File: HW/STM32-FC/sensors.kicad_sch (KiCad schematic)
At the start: 18 parts, among them J5 JST ZH 1.5mm 2P, U6 BMI323, U7 ICM-42688-P, U8 LIS2MDLTR, U9 LPS22HH

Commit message: 2025.02.06 PCB routing done v2
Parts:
- C21, C23, C28, C29: LCSC C1525 -> C1581
- C22: LCSC C1525 -> C26409
- C24: LCSC C1525 -> C1531
- C26: LCSC (none) -> C29823
- C27: LCSC C1525 -> C40894
- C30: LCSC C1525 -> C1770
- J5: LCSC (none) -> C265329
- R16: LCSC (none) -> C25531
- R17: LCSC (none) -> C25539
- R18: LCSC (none) -> C11702
- U6: LCSC (none) -> C5368700
- U7: LCSC (none) -> C1850418
- U8: LCSC (none) -> C919695
- U9: LCSC (none) -> C2827824
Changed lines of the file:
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@@
 			)
 		)
-		(property "LCSC" "C1525"
+		(property "LCSC" "C1531"
 			(at 102.87 40.6462 0)
 			(effects
@@
 			)
 		)
+		(property "LCSC" "C265329"
+			(at 219.71 68.58 0)
+			(effects
+				(font
+					(size 1.27 1.27)
+				)
+				(hide yes)
+			)
+		)
 		(pin "1"
 		)
@@
 			)
 		)
-		(property "LCSC" "C1525"
+		(property "LCSC" "C1581"
 			(at 49.53 128.2762 0)
 			(effects
@@
 			)
 		)
+		(property "LCSC" "C25539"
+			(at 236.22 34.29 0)
+			(effects
+				(font
+					(size 1.27 1.27)
+				)
+				(hide yes)
+			)
+		)
 		(pin "1"
 		)
@@
 			)
 		)
-		(property "LCSC" "C1525"
+		(property "LCSC" "C1770"
 			(at 182.88 68.5862 0)
 			(effects
@@
 			)
 		)
-		(property "LCSC" "C1525"
+		(property "LCSC" "C26409"
 			(at 92.71 40.6462 0)
 			(effects
@@
 			)
 		)
-		(property "LCSC" "C1525"
+		(property "LCSC" "C1581"
 			(at 93.98 137.1538 0)
 			(effects
@@
 			)
 		)
+		(property "LCSC" "C29823"
+			(at 147.32 125.73 0)
+			(effects
+				(font
+					(size 1.27 1.27)
+				)
+				(hide yes)
+			)
+		)
 		(pin "2"
 		)
@@
 			)
 		)
+		(property "LCSC" "C1850418"
+			(at 64.77 50.8 0)
+			(effects
+				(font
+					(size 1.27 1.27)
+				)
+				(hide yes)
+			)
+		)
 		(pin "7"
 		)
@@
 			)
 		)
-		(property "LCSC" "C1525"
+		(property "LCSC" "C1581"
 			(at 181.61 33.0262 0)
 			(effects
@@
 			)
 		)
+		(property "LCSC" "C919695"
+			(at 157.48 64.77 0)
+			(effects
+				(font
+					(size 1.27 1.27)
+				)
+				(hide yes)
+			)
+		)
 		(pin "1"
 		)
@@
 			)
 		)
+		(property "LCSC" "C25531"
+			(at 189.23 121.92 0)
+			(effects
+				(font
+					(size 1.27 1.27)
+				)
+				(hide yes)
+			)
+		)
 		(pin "1"
 		)
@@
 			)
 		)
+		(property "LCSC" "C2827824"
+			(at 161.29 127 0)
+			(effects
+				(font
+					(size 1.27 1.27)
+				)
+				(hide yes)
+			)
+		)
 		(pin "7"
 		)
@@
 			)
 		)
-		(property "LCSC" "C1525"
+		(property "LCSC" "C40894"
 			(at 158.75 33.0262 0)
 			(effects
@@
 			)
 		)
+		(property "LCSC" "C5368700"
+			(at 53.34 115.57 0)
+			(effects
+				(font
+					(size 1.27 1.27)
+				)
+				(hide yes)
+			)
+		)
 		(pin "13"
 		)
@@
 			)
 		)
-		(property "LCSC" "C1525"
+		(property "LCSC" "C1581"
 			(at 170.18 33.0262 0)
 			(effects
@@
 			(at 236.22 44.45 0)
 			(effects
+				(font
+					(size 1.27 1.27)
+				)
+				(hide yes)
+			)
+		)
+		(property "LCSC" "C11702"
+			(at 236.22 44.45 0)
+			(effects

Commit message: 2025.02.06 PCB routing done v3
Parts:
- C25: LCSC C1525 -> C1524
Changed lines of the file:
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@@
 			)
 		)
+		(property "JLC" ""
+			(at 100.33 41.91 0)
+			(effects
+				(font
+					(size 1.27 1.27)
+				)
+				(hide yes)
+			)
+		)
 		(pin "1"
 		)
@@
 			)
 		)
+		(property "JLC" ""
+			(at 219.71 68.58 0)
+			(effects
+				(font
+					(size 1.27 1.27)
+				)
+				(hide yes)
+			)
+		)
 		(pin "1"
 		)
@@
 			)
 		)
+		(property "JLC" ""
+			(at 46.99 129.54 0)
+			(effects
+				(font
+					(size 1.27 1.27)
+				)
+				(hide yes)
+			)
+		)
 		(pin "1"
 		)
@@
 			)
 		)
+		(property "JLC" ""
+			(at 236.22 34.29 0)
+			(effects
+				(font
+					(size 1.27 1.27)
+				)
+				(hide yes)
+			)
+		)
 		(pin "1"
 		)
@@
 			)
 		)
-		(property "LCSC" "C1525"
+		(property "LCSC" "C1524"
 			(at 113.03 40.6462 0)
 			(effects
@@
 			)
 		)
+		(property "JLC" ""
+			(at 110.49 41.91 0)
+			(effects
+				(font
+					(size 1.27 1.27)
+				)
+				(hide yes)
+			)
+		)
 		(pin "1"
 		)
@@
 			)
 		)
+		(property "JLC" ""
+			(at 180.34 69.85 0)
+			(effects
+				(font
+					(size 1.27 1.27)
+				)
+				(hide yes)
+			)
+		)
 		(pin "1"
 		)
@@
 			)
 		)
+		(property "JLC" ""
+			(at 90.17 41.91 0)
+			(effects
+				(font
+					(size 1.27 1.27)
+				)
+				(hide yes)
+			)
+		)
 		(pin "1"
 		)
@@
 			)
 		)
+		(property "JLC" ""
+			(at 96.52 135.89 0)
+			(effects
+				(font
+					(size 1.27 1.27)
+				)
+				(hide yes)
+			)
+		)
 		(pin "1"
 		)
@@
 			)
 		)
+		(property "JLC" ""
+			(at 147.32 125.73 0)
+			(effects
+				(font
+					(size 1.27 1.27)
+				)
+				(hide yes)
+			)
+		)
 		(pin "2"
 		)
@@
 			)
 		)
+		(property "JLC" ""
+			(at 64.77 50.8 0)
+			(effects
+				(font
+					(size 1.27 1.27)
+				)
+				(hide yes)
+			)
+		)
 		(pin "7"
 		)
@@
 			)
 		)
+		(property "JLC" ""
+			(at 179.07 34.29 0)
+			(effects
+				(font
+					(size 1.27 1.27)
+				)
+				(hide yes)
+			)
+		)
 		(pin "1"
 		)
@@
 			)
 		)
+		(property "JLC" ""
+			(at 157.48 64.77 0)
+			(effects
+				(font
+					(size 1.27 1.27)
+				)
+				(hide yes)
+			)
+		)
 		(pin "1"
 		)
@@
 			)
 		)
+		(property "JLC" ""
+			(at 189.23 121.92 0)
+			(effects
+				(font
+					(size 1.27 1.27)
+				)
+				(hide yes)
+			)
+		)
 		(pin "1"
 		)
@@
 			)
 		)
+		(property "JLC" ""
+			(at 161.29 127 0)
+			(effects
+				(font
+					(size 1.27 1.27)
+				)
+				(hide yes)
+			)
+		)
 		(pin "7"
 		)
@@
 			)
 		)
+		(property "JLC" ""
+			(at 156.21 34.29 0)
+			(effects
+				(font
+					(size 1.27 1.27)
+				)
+				(hide yes)
+			)
+		)
 		(pin "1"
 		)
@@
 			)
 		)
+		(property "JLC" ""
+			(at 53.34 115.57 0)
+			(effects
+				(font
+					(size 1.27 1.27)
+				)
+				(hide yes)
+			)
+		)
 		(pin "13"
 		)
@@
 			)
 		)
+		(property "JLC" ""
+			(at 167.64 34.29 0)
+			(effects
+				(font
+					(size 1.27 1.27)
+				)
+				(hide yes)
+			)
+		)
 		(pin "1"
 		)
@@
 			(at 236.22 44.45 0)
 			(effects
+				(font
+					(size 1.27 1.27)
+				)
+				(hide yes)
+			)
+		)
+		(property "JLC" ""
+			(at 236.22 44.45 0)
+			(effects

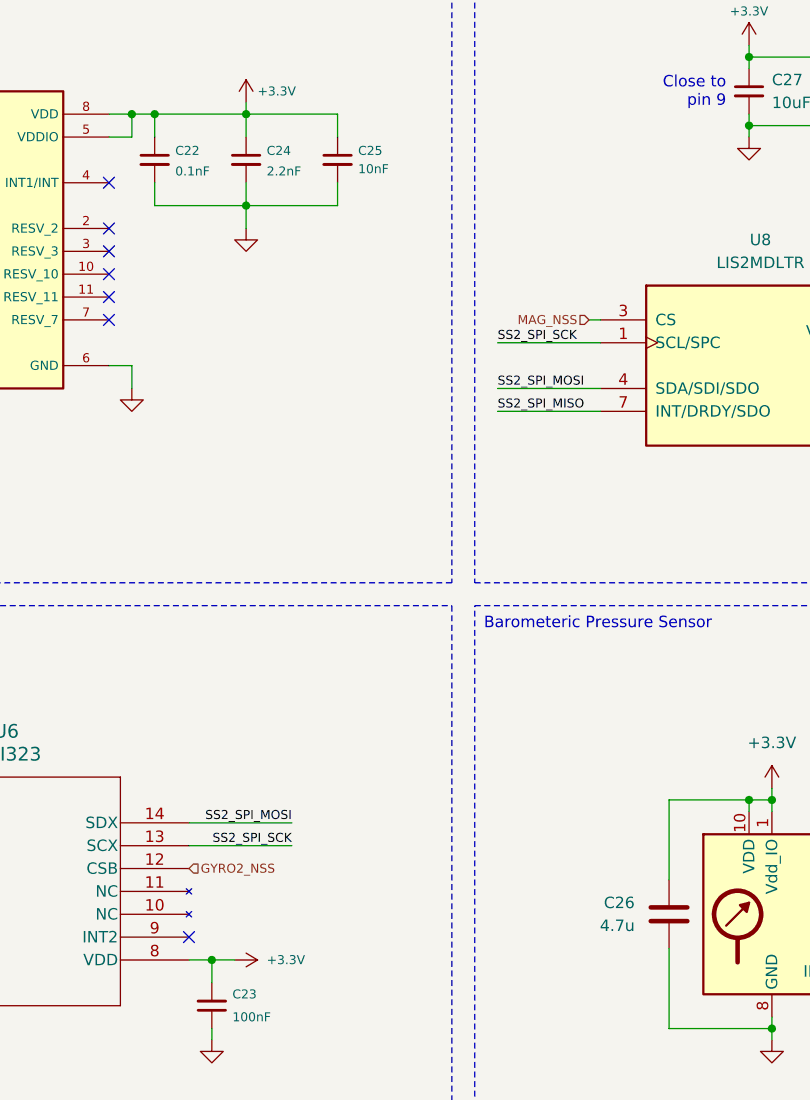
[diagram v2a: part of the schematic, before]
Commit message: 2025.02.07 USB C Conn change v1
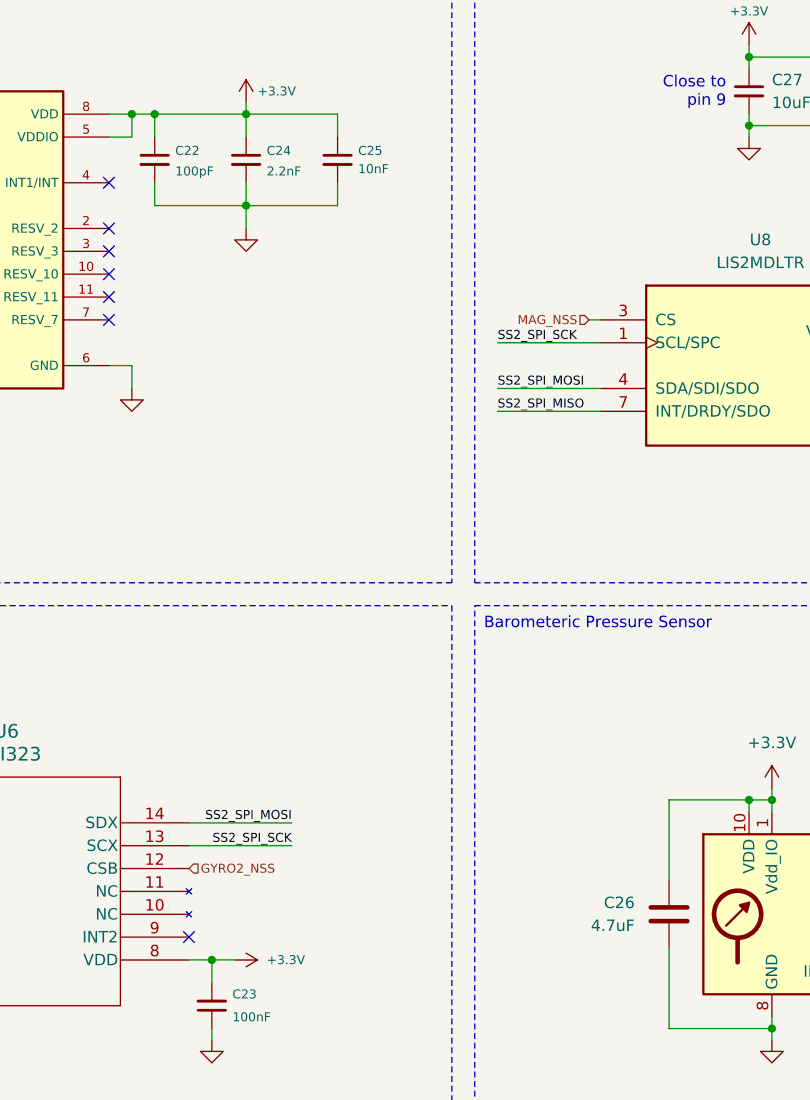
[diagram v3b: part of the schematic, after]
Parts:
- C21, C23, C28, C29: LCSC C1581 -> C1525
- C22: value 0.1nF -> 100pF; LCSC C26409 -> C152819
- C24: LCSC C1531 -> C84703
- C25: LCSC C1524 -> C15195
- C26: value 4.7u -> 4.7uF; LCSC C29823 -> C368809
- C27: LCSC C40894 -> C77000
- C30: LCSC C1770 -> C16651
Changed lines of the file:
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@@
 			)
 		)
-		(property "LCSC" "C1531"
+		(property "LCSC" "C84703"
 			(at 102.87 40.6462 0)
 			(effects
@@
 			)
 		)
-		(property "LCSC" "C1581"
+		(property "LCSC" "C1525"
 			(at 49.53 128.2762 0)
 			(effects
@@
 			)
 		)
-		(property "LCSC" "C1524"
+		(property "LCSC" "C15195"
 			(at 113.03 40.6462 0)
 			(effects
@@
 			)
 		)
-		(property "LCSC" "C1770"
+		(property "LCSC" "C16651"
 			(at 182.88 68.5862 0)
 			(effects
@@
 			)
 		)
-		(property "Value" "0.1nF"
+		(property "Value" "100pF"
 			(at 92.456 43.18 0)
 			(effects
@@
 			)
 		)
-		(property "LCSC" "C26409"
+		(property "LCSC" "C152819"
 			(at 92.71 40.6462 0)
 			(effects
@@
 			)
 		)
-		(property "LCSC" "C1581"
+		(property "LCSC" "C1525"
 			(at 93.98 137.1538 0)
 			(effects
@@
 			)
 		)
-		(property "Value" "4.7u"
+		(property "Value" "4.7uF"
 			(at 143.51 127 0)
 			(effects
@@
 			)
 		)
-		(property "LCSC" "C29823"
+		(property "LCSC" "C368809"
 			(at 147.32 125.73 0)
 			(effects
@@
 			)
 		)
-		(property "LCSC" "C1581"
+		(property "LCSC" "C1525"
 			(at 181.61 33.0262 0)
 			(effects
@@
 			)
 		)
-		(property "LCSC" "C40894"
+		(property "LCSC" "C77000"
 			(at 158.75 33.0262 0)
 			(effects
@@
 			)
 		)
-		(property "LCSC" "C1581"
+		(property "LCSC" "C1525"
 			(at 170.18 33.0262 0)
 			(effects

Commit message: 2025.02.11 PCB DONE! MEMO UPDATING
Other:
- note added: "JST ZH 1.5mm 2P V_BATT : PC0 : ADC123_IN10"
- note added: "SPI1_SCK : PA5 SPI1_MISO : PA6 SPI1_MOSI : PA7 BARO_NSS : PE6 BARO_INT : PE7"
- note added: "SPI1_SCK : PA5 SPI1_MISO : PA6 SPI1_MOSI : PA7 GYRO1_NSS : PE5"
- note added: "SPI3_SCK : PB3 SPI3_MISO : PB4 SPI3_MOSI : PB5 GYRO2_NSS : PE3"
- note added: "SPI3_SCK : PB3 SPI3_MISO : PB4 SPI3_MOSI : PB5 MAG_NSS : PE4"
- note removed: "JST ZH 1.5mm 2P PC1 : ADC123_IN11"
- moved on the sheet: R17, R18
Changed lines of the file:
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@@
 	(title_block
 		(title "Sensors")
-		(date "2025-02-05")
+		(date "2025-02-08")
 		(rev "A")
 		(company "NARAE")
@@
 	)
 	(junction
-		(at 236.22 39.37)
+		(at 236.22 41.91)
 		(diameter 0)
 		(color 0 0 0 0)
@@
 	(wire
 		(pts
-			(xy 236.22 46.99) (xy 236.22 48.26)
+			(xy 236.22 49.53) (xy 236.22 50.8)
 		)
 		(stroke
@@
 	(wire
 		(pts
-			(xy 236.22 39.37) (xy 236.22 41.91)
+			(xy 236.22 41.91) (xy 236.22 44.45)
 		)
 		(stroke
@@
 	(wire
 		(pts
-			(xy 236.22 39.37) (xy 228.6 39.37)
+			(xy 236.22 41.91) (xy 228.6 41.91)
 		)
 		(stroke
@@
 	(wire
 		(pts
-			(xy 236.22 36.83) (xy 236.22 39.37)
+			(xy 236.22 39.37) (xy 236.22 41.91)
 		)
 		(stroke
@@
 	(wire
 		(pts
-			(xy 236.22 30.48) (xy 236.22 31.75)
+			(xy 236.22 33.02) (xy 236.22 34.29)
 		)
 		(stroke
@@
 		)
 	)
-	(text "JST ZH 1.5mm 2P\n\nPC1 : ADC123_IN11"
+	(text "SPI3_SCK  : PB3\nSPI3_MISO : PB4\nSPI3_MOSI : PB5\n\nGYRO2_NSS : PE3"
+		(exclude_from_sim no)
+		(at 23.876 96.774 0)
+		(effects
+			(font
+				(size 1.27 1.27)
+			)
+			(justify left top)
+		)
+	)
+	(text "SPI1_SCK  : PA5\nSPI1_MISO : PA6\nSPI1_MOSI : PA7\n\nBARO_NSS : PE6\nBARO_INT : PE7"
+		(exclude_from_sim no)
+		(at 126.746 96.774 0)
+		(effects
+			(font
+				(size 1.27 1.27)
+			)
+			(justify left top)
+		)
+	)
+	(text "JST ZH 1.5mm 2P\n\nV_BATT : PC0 : ADC123_IN10"
 		(exclude_from_sim no)
 		(at 208.026 18.034 0)
@@
 		)
 	)
+	(text "SPI1_SCK  : PA5\nSPI1_MISO : PA6\nSPI1_MOSI : PA7\n\nGYRO1_NSS : PE5"
+		(exclude_from_sim no)
+		(at 23.876 18.034 0)
+		(effects
+			(font
+				(size 1.27 1.27)
+			)
+			(justify left top)
+		)
+	)
 	(text "Accelerometer/Gyroscope2"
 		(exclude_from_sim no)
@@
 		)
 	)
+	(text "SPI3_SCK  : PB3\nSPI3_MISO : PB4\nSPI3_MOSI : PB5\n\nMAG_NSS : PE4"
+		(exclude_from_sim no)
+		(at 126.746 18.034 0)
+		(effects
+			(font
+				(size 1.27 1.27)
+			)
+			(justify left top)
+		)
+	)
 	(label "SS2_SPI_MOSI"
 		(at 62.23 171.45 180)
@@
 	(hierarchical_label "V_BATT"
 		(shape output)
-		(at 228.6 39.37 180)
+		(at 228.6 41.91 180)
 		(effects
 			(font
@@
 	(symbol
 		(lib_id "Device:R_Small_US")
-		(at 236.22 34.29 0)
+		(at 236.22 36.83 0)
 		(unit 1)
 		(exclude_from_sim no)
@@
 		(dnp no)
 		(property "Reference" "R17"
-			(at 238.506 33.274 0)
+			(at 238.506 35.814 0)
 			(effects
 				(font
@@
 		)
 		(property "Value" "15k"
-			(at 238.506 35.306 0)
+			(at 238.506 37.846 0)
 			(effects
 				(font
@@
 		)
 		(property "Footprint" "Resistor_SMD:R_0402_1005Metric"
-			(at 236.22 34.29 0)
+			(at 236.22 36.83 0)
 			(effects
 				(font
@@
 		)
 		(property "Datasheet" "~"
-			(at 236.22 34.29 0)
+			(at 236.22 36.83 0)
 			(effects
 				(font
@@
 		)
 		(property "Description" "Resistor, small US symbol"
-			(at 236.22 34.29 0)
+			(at 236.22 36.83 0)
 			(effects
 				(font
@@
 		)
 		(property "Availability" ""
-			(at 236.22 34.29 0)
+			(at 236.22 36.83 0)
 			(effects
 				(font
@@
 		)
 		(property "Check_prices" ""
-			(at 236.22 34.29 0)
+			(at 236.22 36.83 0)
 			(effects
 				(font
@@
 		)
 		(property "Description_1" ""
-			(at 236.22 34.29 0)
+			(at 236.22 36.83 0)
 			(effects
 				(font
@@
 		)
 		(property "MF" ""
-			(at 236.22 34.29 0)
+			(at 236.22 36.83 0)
 			(effects
 				(font
@@
 		)
 		(property "MP" ""
-			(at 236.22 34.29 0)
+			(at 236.22 36.83 0)
 			(effects
 				(font
@@
 		)
 		(property "Package" ""
-			(at 236.22 34.29 0)
+			(at 236.22 36.83 0)
 			(effects
 				(font
@@
 		)
 		(property "Price" ""
-			(at 236.22 34.29 0)
+			(at 236.22 36.83 0)
 			(effects
 				(font
@@
 		)
 		(property "SnapEDA_Link" ""
-			(at 236.22 34.29 0)
+			(at 236.22 36.83 0)
 			(effects
 				(font
@@
 		)
 		(property "Sim.Device" ""
-			(at 236.22 34.29 0)
+			(at 236.22 36.83 0)
 			(effects
 				(font
@@
 		)
 		(property "Sim.Pins" ""
-			(at 236.22 34.29 0)
+			(at 236.22 36.83 0)
 			(effects
 				(font
@@
 		)
 		(property "LCSC" "C25539"
-			(at 236.22 34.29 0)
+			(at 236.22 36.83 0)
 			(effects
 				(font
@@
 		)
 		(property "JLC" ""
-			(at 236.22 34.29 0)
+			(at 236.22 36.83 0)
 			(effects
 				(font
@@
 	(symbol
 		(lib_id "power:GND")
-		(at 236.22 48.26 0)
+		(at 236.22 50.8 0)
 		(unit 1)
 		(exclude_from_sim no)
@@
 		(fields_autoplaced yes)
 		(property "Reference" "#PWR068"
-			(at 236.22 54.61 0)
+			(at 236.22 57.15 0)
 			(effects
 				(font
@@
 		)
 		(property "Value" "GND"
-			(at 236.22 53.34 0)
+			(at 236.22 55.88 0)
 			(effects
 				(font
@@
 		)
 		(property "Footprint" ""
-			(at 236.22 48.26 0)
+			(at 236.22 50.8 0)
 			(effects
 				(font
@@
 		)
 		(property "Datasheet" ""
-			(at 236.22 48.26 0)
+			(at 236.22 50.8 0)
 			(effects
 				(font
@@
 		)
 		(property "Description" "Power symbol creates a global label with name \"GND\" , ground"
-			(at 236.22 48.26 0)
+			(at 236.22 50.8 0)
 			(effects
 				(font
@@
 	(symbol
 		(lib_id "power:+BATT")
-		(at 236.22 30.48 0)
+		(at 236.22 33.02 0)
 		(unit 1)
 		(exclude_from_sim no)
@@
 		(fields_autoplaced yes)
 		(property "Reference" "#PWR067"
-			(at 236.22 34.29 0)
+			(at 236.22 36.83 0)
 			(effects
 				(font
@@
 		)
 		(property "Value" "+BATT"
-			(at 236.22 25.4 0)
+			(at 236.22 27.94 0)
 			(effects
 				(font
@@
 		)
 		(property "Footprint" ""
-			(at 236.22 30.48 0)
+			(at 236.22 33.02 0)
 			(effects
 				(font
@@
 		)
 		(property "Datasheet" ""
-			(at 236.22 30.48 0)
+			(at 236.22 33.02 0)
 			(effects
 				(font
@@
 		)
 		(property "Description" "Power symbol creates a global label with name \"+BATT\""
-			(at 236.22 30.48 0)
+			(at 236.22 33.02 0)
 			(effects
 				(font
@@
 	(symbol
 		(lib_id "Device:R_Small_US")
-		(at 236.22 44.45 0)
+		(at 236.22 46.99 0)
 		(unit 1)
 		(exclude_from_sim no)
@@
 		(dnp no)
 		(property "Reference" "R18"
-			(at 238.506 43.688 0)
+			(at 238.506 46.228 0)
 			(effects
 				(font
@@
 		)
 		(property "Value" "1k"
-			(at 238.506 45.466 0)
+			(at 238.506 48.006 0)
 			(effects
 				(font
@@
 		)
 		(property "Footprint" "Resistor_SMD:R_0402_1005Metric"
-			(at 236.22 44.45 0)
+			(at 236.22 46.99 0)
 			(effects
 				(font
@@
 		)
 		(property "Datasheet" "~"
-			(at 236.22 44.45 0)
+			(at 236.22 46.99 0)
 			(effects
 				(font
@@
 		)
 		(property "Description" "Resistor, small US symbol"
-			(at 236.22 44.45 0)
+			(at 236.22 46.99 0)
 			(effects
 				(font
@@
 		)
 		(property "Availability" ""
-			(at 236.22 44.45 0)
+			(at 236.22 46.99 0)
 			(effects
 				(font
@@
 		)
 		(property "Check_prices" ""
-			(at 236.22 44.45 0)
+			(at 236.22 46.99 0)
 			(effects
 				(font
@@
 		)
 		(property "Description_1" ""
-			(at 236.22 44.45 0)
+			(at 236.22 46.99 0)
 			(effects
 				(font
@@
 		)
 		(property "MF" ""
-			(at 236.22 44.45 0)
+			(at 236.22 46.99 0)
 			(effects
 				(font
@@
 		)
 		(property "MP" ""
-			(at 236.22 44.45 0)
+			(at 236.22 46.99 0)
 			(effects
 				(font
@@
 		)
 		(property "Package" ""
-			(at 236.22 44.45 0)
+			(at 236.22 46.99 0)
 			(effects
 				(font
@@
 		)
 		(property "Price" ""
-			(at 236.22 44.45 0)
+			(at 236.22 46.99 0)
 			(effects
 				(font
@@
 		)
 		(property "SnapEDA_Link" ""
-			(at 236.22 44.45 0)
+			(at 236.22 46.99 0)
 			(effects
 				(font
@@
 		)
 		(property "Sim.Device" ""
-			(at 236.22 44.45 0)
+			(at 236.22 46.99 0)
 			(effects
 				(font
@@
 		)
 		(property "Sim.Pins" ""
-			(at 236.22 44.45 0)
+			(at 236.22 46.99 0)
 			(effects
 				(font
@@
 		)
 		(property "LCSC" "C11702"
-			(at 236.22 44.45 0)
+			(at 236.22 46.99 0)
 			(effects
 				(font
@@
 		)
 		(property "JLC" ""
-			(at 236.22 44.45 0)
+			(at 236.22 46.99 0)
 			(effects
 				(font

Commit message: Test software v1
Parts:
- renumbered C21 to C22, C22 to C23, C23 to C24, C24 to C25, C25 to C26, C26 to C27, C27 to C28, C28 to C29, C29 to C30, C30 to C31, R16 to R17, R17 to R18, R18 to R19
